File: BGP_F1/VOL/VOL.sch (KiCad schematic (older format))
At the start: 26 parts, among them P1 CONN_01X05, P2 CONN_01X05, P3 CONN_01X05, P4 CONN_01X03, P5 CONN_01X02, P6 CONN_02X02, P7 CONN_01X12, U1 MC33178, U2 MC33178

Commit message: F1 VOL Prot Diode
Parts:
- added D1: 1N4148, Diodes_SMD:D_SOD-123, symbol D_Small_ALT
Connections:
- net Earth: now also D1.2 (A)
- net V+: now also D1.1 (K)
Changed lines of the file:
@@
 LIBS:contrib
 LIBS:valves
-LIBS:vol-cache
+LIBS:VOL-cache
 EELAYER 25 0
 EELAYER END
@@
 Text Label 8400 3300 1    60   ~ 0
 V+
+$Comp
+L D_Small_ALT D1
+U 1 1 5A5F9F82
+P 8700 3400
+F 0 "D1" H 8650 3480 50  0000 L CNN
+F 1 "1N4148" H 8550 3320 50  0000 L CNN
+F 2 "Diodes_SMD:D_SOD-123" V 8700 3400 50  0001 C CNN
+F 3 "" V 8700 3400 50  0001 C CNN
+	1    8700 3400
+	0    1    1    0
+$EndComp
+Wire Wire Line
+	8400 3500 8700 3500
+Wire Wire Line
+	8400 3300 8700 3300
 $EndSCHEMATC

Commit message: F boards routed, various optimisations made
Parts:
- D1: footprint Diodes_SMD:D_SOD-123 -> Diodes_SMD:DO-214BA
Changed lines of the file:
@@
 F 0 "D1" H 8650 3480 50  0000 L CNN
 F 1 "1N4148" H 8550 3320 50  0000 L CNN
-F 2 "Diodes_SMD:D_SOD-123" V 8700 3400 50  0001 C CNN
+F 2 "Diodes_SMD:DO-214BA" V 8700 3400 50  0001 C CNN
 F 3 "" V 8700 3400 50  0001 C CNN
 	1    8700 3400

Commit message: F VOL
POT EARTH FIXUP
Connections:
- net Earth: now also P7.10 (P10)
- net Vref: no longer P7.10 (P10)
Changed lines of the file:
@@
 Text Label 9400 3350 2    60   ~ 0
 PV_3
-Text Label 9400 3150 2    60   ~ 0
-Vref
 Text Label 2650 4750 0    60   ~ 0
 V+
@@
 Wire Wire Line
 	8400 3300 8700 3300
+$Comp
+L Earth #PWR?
+U 1 1 5A606171
+P 9400 3150
+F 0 "#PWR?" H 9400 2900 50  0001 C CNN
+F 1 "Earth" H 9400 3000 50  0001 C CNN
+F 2 "" H 9400 3150 50  0000 C CNN
+F 3 "" H 9400 3150 50  0000 C CNN
+	1    9400 3150
+	0    1    1    0
+$EndComp
 $EndSCHEMATC

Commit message: Updated F_VOL
Using 10kB, 100kA pot with correct orientation, and pot correction for blend.
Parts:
- R3, R4: value 4.99k -> 11.1k
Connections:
- net PB1_1: now also P7.3 (P3); no longer P7.1 (P1)
- net PB1_2: no longer R3.1
- net PB2_2: no longer R4.1
- net Vref: now also P7.1 (P1), P7.6 (P6), R3.1, R4.1; no longer P7.3 (P3), P7.4 (P4)
- net PB2_3 renamed PB2_1
- net PB2_1: now also P7.4 (P4); no longer P7.6 (P6)
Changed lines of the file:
@@
 V+
 $Comp
-L Earth #PWR01
+L Earth #PWR5
 U 1 1 5A5EC7CD
 P 4150 3200
-F 0 "#PWR01" H 4150 2950 50  0001 C CNN
+F 0 "#PWR5" H 4150 2950 50  0001 C CNN
 F 1 "Earth" H 4150 3050 50  0001 C CNN
 F 2 "" H 4150 3200 50  0000 C CNN
@@
 Text Label 3650 3900 3    60   ~ 0
 Vref
-$Comp
-L R_Small R3
-U 1 1 5A5EC802
-P 4800 3500
-F 0 "R3" H 4830 3520 50  0000 L CNN
-F 1 "4.99k" H 4830 3460 50  0000 L CNN
-F 2 "Resistors_SMD:R_0603_HandSoldering" H 4800 3500 50  0001 C CNN
-F 3 "" H 4800 3500 50  0000 C CNN
-	1    4800 3500
-	0    1    1    0
-$EndComp
 Text Label 4700 3500 1    60   ~ 0
 PB1_1
-Text Label 5050 3500 1    60   ~ 0
+Text Label 4900 3500 1    60   ~ 0
 PB1_2
 Text Label 3650 3600 2    60   ~ 0
@@
 V+
 $Comp
-L Earth #PWR02
+L Earth #PWR6
 U 1 1 5A5EC9DD
 P 4150 4200
-F 0 "#PWR02" H 4150 3950 50  0001 C CNN
+F 0 "#PWR6" H 4150 3950 50  0001 C CNN
 F 1 "Earth" H 4150 4050 50  0001 C CNN
 F 2 "" H 4150 4200 50  0000 C CNN
@@
 Text Label 3650 4900 3    60   ~ 0
 Vref
-$Comp
-L R_Small R4
-U 1 1 5A5EC9E9
-P 4800 4500
-F 0 "R4" H 4830 4520 50  0000 L CNN
-F 1 "4.99k" H 4830 4460 50  0000 L CNN
-F 2 "Resistors_SMD:R_0603_HandSoldering" H 4800 4500 50  0001 C CNN
-F 3 "" H 4800 4500 50  0000 C CNN
-	1    4800 4500
-	0    1    1    0
-$EndComp
-Text Label 5050 4500 1    60   ~ 0
+Text Label 4900 4500 1    60   ~ 0
 PB2_2
 Text Label 3650 4600 2    60   ~ 0
@@
 V+
 $Comp
-L Earth #PWR03
+L Earth #PWR7
 U 1 1 5A5ECE8B
 P 5850 2750
-F 0 "#PWR03" H 5850 2500 50  0001 C CNN
+F 0 "#PWR7" H 5850 2500 50  0001 C CNN
 F 1 "Earth" H 5850 2600 50  0001 C CNN
 F 2 "" H 5850 2750 50  0000 C CNN
@@
 $EndComp
 $Comp
-L Earth #PWR04
+L Earth #PWR8
 U 1 1 5A5ED3C7
 P 6800 3600
-F 0 "#PWR04" H 6800 3350 50  0001 C CNN
+F 0 "#PWR8" H 6800 3350 50  0001 C CNN
 F 1 "Earth" H 6800 3450 50  0001 C CNN
 F 2 "" H 6800 3600 50  0000 C CNN
@@
 V+
 $Comp
-L Earth #PWR05
+L Earth #PWR10
 U 1 1 5A5EDC55
 P 7950 2650
-F 0 "#PWR05" H 7950 2400 50  0001 C CNN
+F 0 "#PWR10" H 7950 2400 50  0001 C CNN
 F 1 "Earth" H 7950 2500 50  0001 C CNN
 F 2 "" H 7950 2650 50  0000 C CNN
@@
 Connection ~ 7450 3050
 $Comp
-L Earth #PWR06
+L Earth #PWR9
 U 1 1 5A5EE012
 P 7450 3550
-F 0 "#PWR06" H 7450 3300 50  0001 C CNN
+F 0 "#PWR9" H 7450 3300 50  0001 C CNN
 F 1 "Earth" H 7450 3400 50  0001 C CNN
 F 2 "" H 7450 3550 50  0000 C CNN
@@
 OUT_N
 $Comp
-L Earth #PWR07
+L Earth #PWR1
 U 1 1 5A5EEAF2
 P 2650 2550
-F 0 "#PWR07" H 2650 2300 50  0001 C CNN
+F 0 "#PWR1" H 2650 2300 50  0001 C CNN
 F 1 "Earth" H 2650 2400 50  0001 C CNN
 F 2 "" H 2650 2550 50  0000 C CNN
@@
 $EndComp
 $Comp
-L Earth #PWR08
+L Earth #PWR2
 U 1 1 5A5EEB70
 P 2650 3150
-F 0 "#PWR08" H 2650 2900 50  0001 C CNN
+F 0 "#PWR2" H 2650 2900 50  0001 C CNN
 F 1 "Earth" H 2650 3000 50  0001 C CNN
 F 2 "" H 2650 3150 50  0000 C CNN
@@
 $EndComp
 $Comp
-L Earth #PWR09
+L Earth #PWR3
 U 1 1 5A5EEBC0
 P 2650 3750
-F 0 "#PWR09" H 2650 3500 50  0001 C CNN
+F 0 "#PWR3" H 2650 3500 50  0001 C CNN
 F 1 "Earth" H 2650 3600 50  0001 C CNN
 F 2 "" H 2650 3750 50  0000 C CNN
@@
 OUT
 $Comp
-L Earth #PWR010
+L Earth #PWR4
 U 1 1 5A5EF35E
 P 2650 4050
-F 0 "#PWR010" H 2650 3800 50  0001 C CNN
+F 0 "#PWR4" H 2650 3800 50  0001 C CNN
 F 1 "Earth" H 2650 3900 50  0001 C CNN
 F 2 "" H 2650 4050 50  0000 C CNN
@@
 	1    0    0    -1
 $EndComp
-Text Label 9400 2250 2    60   ~ 0
+Text Label 9400 2450 2    60   ~ 0
 PB1_1
 Text Label 9400 2350 2    60   ~ 0
@@
 Text Label 9400 2650 2    60   ~ 0
 PB2_2
-Text Label 9400 2750 2    60   ~ 0
-PB2_3
+Text Label 9400 2550 2    60   ~ 0
+PB2_1
 Text Label 9400 3250 2    60   ~ 0
 PV_2
@@
 BUF_N
 Text Label 4700 4500 1    60   ~ 0
-PB2_3
-Text Label 9400 2450 2    60   ~ 0
-Vref
-Text Label 9400 2550 2    60   ~ 0
+PB2_1
+Text Label 9400 2250 2    60   ~ 0
+Vref
+Text Label 9400 2750 2    60   ~ 0
 Vref
 Text Label 9400 3350 2    60   ~ 0
@@
 $EndComp
 $Comp
-L Earth #PWR011
+L Earth #PWR11
 U 1 1 5A5F15E8
 P 8400 3500
-F 0 "#PWR011" H 8400 3250 50  0001 C CNN
+F 0 "#PWR11" H 8400 3250 50  0001 C CNN
 F 1 "Earth" H 8400 3350 50  0001 C CNN
 F 2 "" H 8400 3500 50  0000 C CNN
@@
 	8400 3300 8700 3300
 $Comp
-L Earth #PWR?
+L Earth #PWR12
 U 1 1 5A606171
 P 9400 3150
-F 0 "#PWR?" H 9400 2900 50  0001 C CNN
+F 0 "#PWR12" H 9400 2900 50  0001 C CNN
 F 1 "Earth" H 9400 3000 50  0001 C CNN
 F 2 "" H 9400 3150 50  0000 C CNN
@@
 	0    1    1    0
 $EndComp
+$Comp
+L R_Small R3
+U 1 1 5A6282A9
+P 4700 3650
+F 0 "R3" H 4730 3670 50  0000 L CNN
+F 1 "11.1k" H 4730 3610 50  0000 L CNN
+F 2 "Resistors_SMD:R_0603_HandSoldering" H 4700 3650 50  0001 C CNN
+F 3 "" H 4700 3650 50  0000 C CNN
+	1    4700 3650
+	-1   0    0    1
+$EndComp
+$Comp
+L R_Small R4
+U 1 1 5A628323
+P 4700 4650
+F 0 "R4" H 4730 4670 50  0000 L CNN
+F 1 "11.1k" H 4730 4610 50  0000 L CNN
+F 2 "Resistors_SMD:R_0603_HandSoldering" H 4700 4650 50  0001 C CNN
+F 3 "" H 4700 4650 50  0000 C CNN
+	1    4700 4650
+	-1   0    0    1
+$EndComp
+Text Label 4700 4800 3    60   ~ 0
+Vref
+Wire Wire Line
+	4700 4800 4700 4750
+Wire Wire Line
+	4700 4500 4700 4550
+Wire Wire Line
+	4700 3500 4700 3550
+Wire Wire Line
+	4700 3800 4700 3750
+Text Label 4700 3800 3    60   ~ 0
+Vref
 $EndSCHEMATC

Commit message: New F0 Version
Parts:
- P1, P2, P3: footprint Connectors_Molex:Molex_MicroLatch-53253-0570_05x2.00mm_Straight -> Connectors_JST:JST_PH_B5B-PH-K_05x2.00mm_Straight
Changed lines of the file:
@@
 V+
 $Comp
-L Earth #PWR5
+L Earth #PWR01
 U 1 1 5A5EC7CD
 P 4150 3200
-F 0 "#PWR5" H 4150 2950 50  0001 C CNN
+F 0 "#PWR01" H 4150 2950 50  0001 C CNN
 F 1 "Earth" H 4150 3050 50  0001 C CNN
 F 2 "" H 4150 3200 50  0000 C CNN
@@
 V+
 $Comp
-L Earth #PWR6
+L Earth #PWR02
 U 1 1 5A5EC9DD
 P 4150 4200
-F 0 "#PWR6" H 4150 3950 50  0001 C CNN
+F 0 "#PWR02" H 4150 3950 50  0001 C CNN
 F 1 "Earth" H 4150 4050 50  0001 C CNN
 F 2 "" H 4150 4200 50  0000 C CNN
@@
 V+
 $Comp
-L Earth #PWR7
+L Earth #PWR03
 U 1 1 5A5ECE8B
 P 5850 2750
-F 0 "#PWR7" H 5850 2500 50  0001 C CNN
+F 0 "#PWR03" H 5850 2500 50  0001 C CNN
 F 1 "Earth" H 5850 2600 50  0001 C CNN
 F 2 "" H 5850 2750 50  0000 C CNN
@@
 $EndComp
 $Comp
-L Earth #PWR8
+L Earth #PWR04
 U 1 1 5A5ED3C7
 P 6800 3600
-F 0 "#PWR8" H 6800 3350 50  0001 C CNN
+F 0 "#PWR04" H 6800 3350 50  0001 C CNN
 F 1 "Earth" H 6800 3450 50  0001 C CNN
 F 2 "" H 6800 3600 50  0000 C CNN
@@
 V+
 $Comp
-L Earth #PWR10
+L Earth #PWR05
 U 1 1 5A5EDC55
 P 7950 2650
-F 0 "#PWR10" H 7950 2400 50  0001 C CNN
+F 0 "#PWR05" H 7950 2400 50  0001 C CNN
 F 1 "Earth" H 7950 2500 50  0001 C CNN
 F 2 "" H 7950 2650 50  0000 C CNN
@@
 Connection ~ 7450 3050
 $Comp
-L Earth #PWR9
+L Earth #PWR06
 U 1 1 5A5EE012
 P 7450 3550
-F 0 "#PWR9" H 7450 3300 50  0001 C CNN
+F 0 "#PWR06" H 7450 3300 50  0001 C CNN
 F 1 "Earth" H 7450 3400 50  0001 C CNN
 F 2 "" H 7450 3550 50  0000 C CNN
@@
 F 0 "P1" H 2450 2650 50  0000 C CNN
 F 1 "CONN_01X05" V 2550 2350 50  0000 C CNN
-F 2 "Connectors_Molex:Molex_MicroLatch-53253-0570_05x2.00mm_Straight" H 2450 2350 50  0001 C CNN
+F 2 "Connectors_JST:JST_PH_B5B-PH-K_05x2.00mm_Straight" H 2450 2350 50  0001 C CNN
 F 3 "" H 2450 2350 50  0000 C CNN
 	1    2450 2350
@@
 F 0 "P2" H 2450 3250 50  0000 C CNN
 F 1 "CONN_01X05" V 2550 2950 50  0000 C CNN
-F 2 "Connectors_Molex:Molex_MicroLatch-53253-0570_05x2.00mm_Straight" H 2450 2950 50  0001 C CNN
+F 2 "Connectors_JST:JST_PH_B5B-PH-K_05x2.00mm_Straight" H 2450 2950 50  0001 C CNN
 F 3 "" H 2450 2950 50  0000 C CNN
 	1    2450 2950
@@
 F 0 "P3" H 2450 3850 50  0000 C CNN
 F 1 "CONN_01X05" V 2550 3550 50  0000 C CNN
-F 2 "Connectors_Molex:Molex_MicroLatch-53253-0570_05x2.00mm_Straight" H 2450 3550 50  0001 C CNN
+F 2 "Connectors_JST:JST_PH_B5B-PH-K_05x2.00mm_Straight" H 2450 3550 50  0001 C CNN
 F 3 "" H 2450 3550 50  0000 C CNN
 	1    2450 3550
@@
 OUT_N
 $Comp
-L Earth #PWR1
+L Earth #PWR07
 U 1 1 5A5EEAF2
 P 2650 2550
-F 0 "#PWR1" H 2650 2300 50  0001 C CNN
+F 0 "#PWR07" H 2650 2300 50  0001 C CNN
 F 1 "Earth" H 2650 2400 50  0001 C CNN
 F 2 "" H 2650 2550 50  0000 C CNN
@@
 $EndComp
 $Comp
-L Earth #PWR2
+L Earth #PWR08
 U 1 1 5A5EEB70
 P 2650 3150
-F 0 "#PWR2" H 2650 2900 50  0001 C CNN
+F 0 "#PWR08" H 2650 2900 50  0001 C CNN
 F 1 "Earth" H 2650 3000 50  0001 C CNN
 F 2 "" H 2650 3150 50  0000 C CNN
@@
 $EndComp
 $Comp
-L Earth #PWR3
+L Earth #PWR09
 U 1 1 5A5EEBC0
 P 2650 3750
-F 0 "#PWR3" H 2650 3500 50  0001 C CNN
+F 0 "#PWR09" H 2650 3500 50  0001 C CNN
 F 1 "Earth" H 2650 3600 50  0001 C CNN
 F 2 "" H 2650 3750 50  0000 C CNN
@@
 OUT
 $Comp
-L Earth #PWR4
+L Earth #PWR010
 U 1 1 5A5EF35E
 P 2650 4050
-F 0 "#PWR4" H 2650 3800 50  0001 C CNN
+F 0 "#PWR010" H 2650 3800 50  0001 C CNN
 F 1 "Earth" H 2650 3900 50  0001 C CNN
 F 2 "" H 2650 4050 50  0000 C CNN
@@
 $EndComp
 $Comp
-L Earth #PWR11
+L Earth #PWR011
 U 1 1 5A5F15E8
 P 8400 3500
-F 0 "#PWR11" H 8400 3250 50  0001 C CNN
+F 0 "#PWR011" H 8400 3250 50  0001 C CNN
 F 1 "Earth" H 8400 3350 50  0001 C CNN
 F 2 "" H 8400 3500 50  0000 C CNN
@@
 	8400 3300 8700 3300
 $Comp
-L Earth #PWR12
+L Earth #PWR012
 U 1 1 5A606171
 P 9400 3150
-F 0 "#PWR12" H 9400 2900 50  0001 C CNN
+F 0 "#PWR012" H 9400 2900 50  0001 C CNN
 F 1 "Earth" H 9400 3000 50  0001 C CNN
 F 2 "" H 9400 3150 50  0000 C CNN

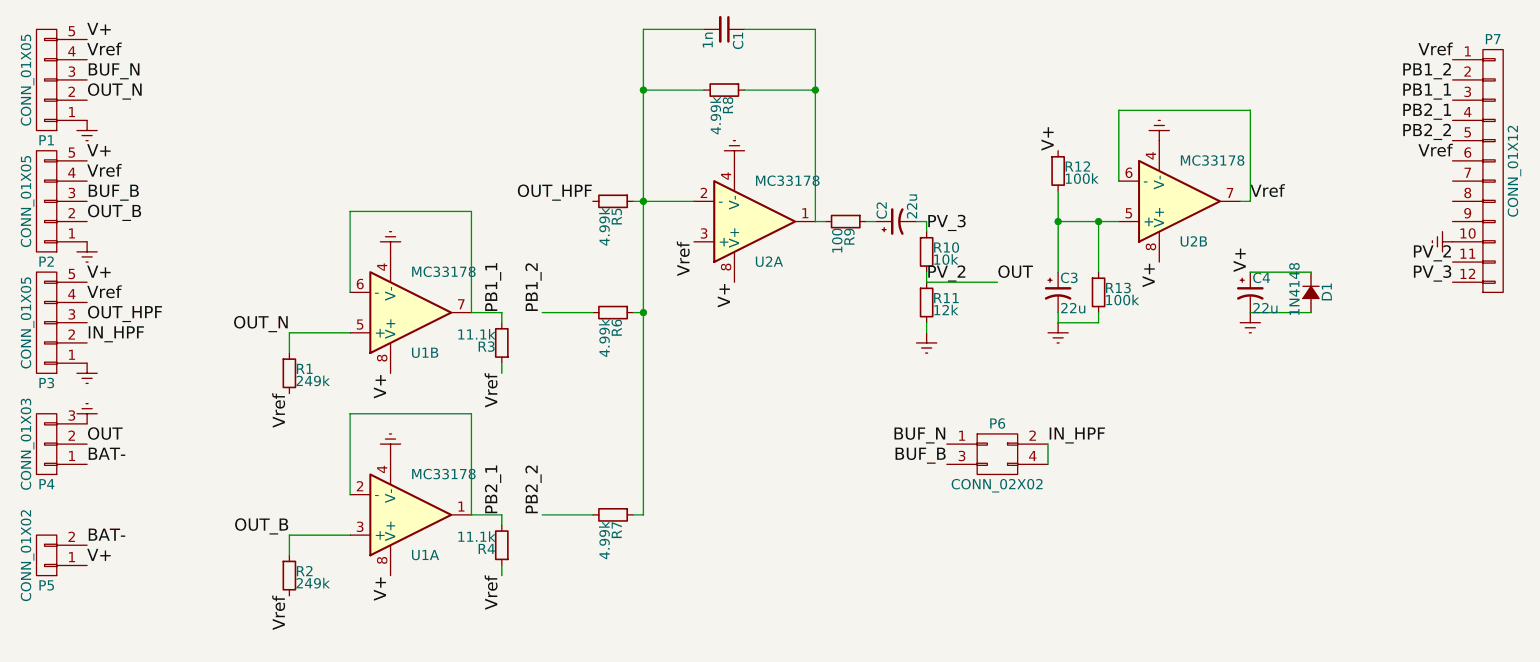
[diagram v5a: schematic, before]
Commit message: F1 updates to reverse pots
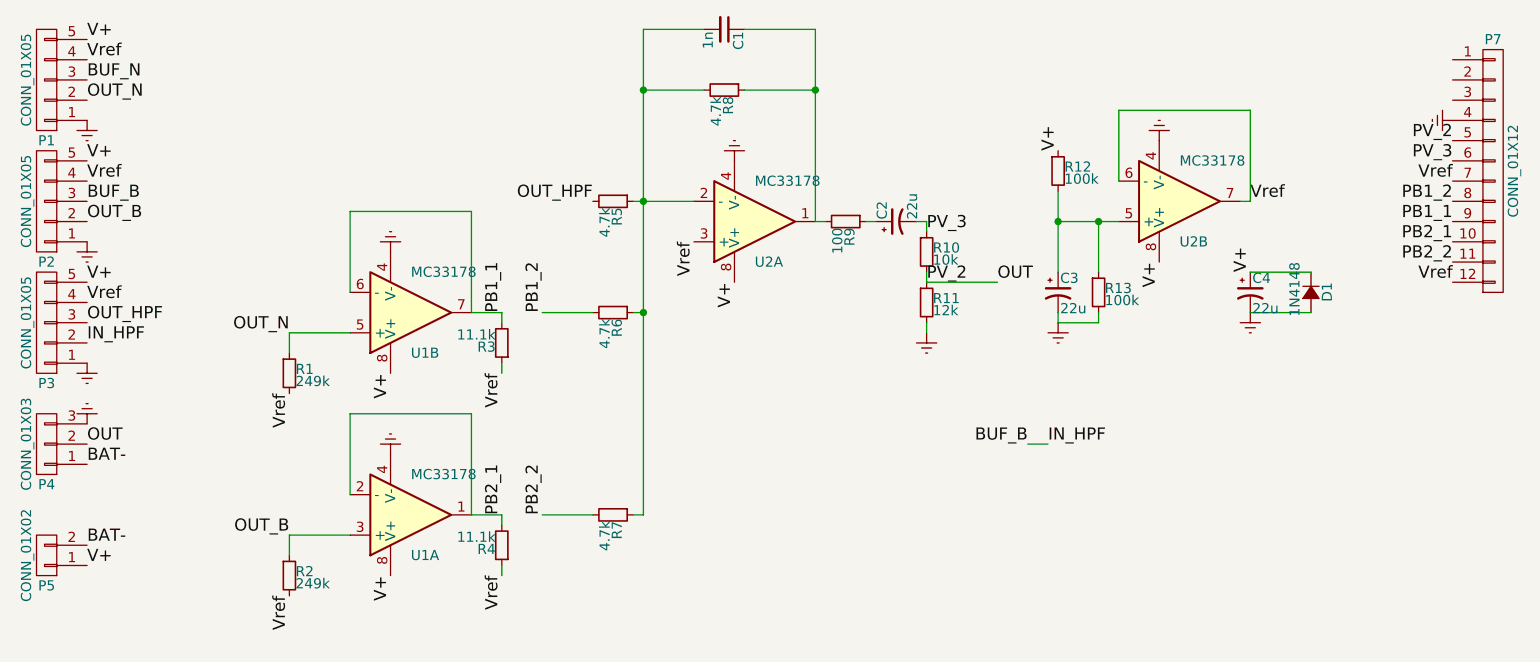
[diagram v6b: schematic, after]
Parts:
- removed P6: CONN_02X02, Pin_Headers:Pin_Header_Straight_2x02, symbol CONN_02X02
- R5, R6, R7, R8: value 4.99k -> 4.7k
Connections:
- net IN_HPF is gone; now on net BUF_B: P3.2 (P2)
- net Earth: now also P7.4 (P4); no longer P7.10 (P10)
- net OUT: now also P7.5 (P5); no longer P7.11 (P11)
- net PB1_1: now also P7.9 (P9); no longer P7.3 (P3)
- net PB1_2: now also P7.8 (P8); no longer P7.2 (P2)
- net PB2_1: now also P7.10 (P10); no longer P7.4 (P4)
- net PB2_2: now also P7.11 (P11); no longer P7.5 (P5)
- net PV_3: now also P7.6 (P6); no longer P7.12 (P12)
- net Vref: now also P7.12 (P12), P7.7 (P7); no longer P7.1 (P1), P7.6 (P6)
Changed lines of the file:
@@
 P 5250 3500
 F 0 "R6" H 5280 3520 50  0000 L CNN
-F 1 "4.99k" H 5280 3460 50  0000 L CNN
+F 1 "4.7k" H 5280 3460 50  0000 L CNN
 F 2 "Resistors_SMD:R_0603_HandSoldering" H 5250 3500 50  0001 C CNN
 F 3 "" H 5250 3500 50  0000 C CNN
@@
 P 5250 4500
 F 0 "R7" H 5280 4520 50  0000 L CNN
-F 1 "4.99k" H 5280 4460 50  0000 L CNN
+F 1 "4.7k" H 5280 4460 50  0000 L CNN
 F 2 "Resistors_SMD:R_0603_HandSoldering" H 5250 4500 50  0001 C CNN
 F 3 "" H 5250 4500 50  0000 C CNN
@@
 P 5250 2950
 F 0 "R5" H 5280 2970 50  0000 L CNN
-F 1 "4.99k" H 5280 2910 50  0000 L CNN
+F 1 "4.7k" H 5280 2910 50  0000 L CNN
 F 2 "Resistors_SMD:R_0603_HandSoldering" H 5250 2950 50  0001 C CNN
 F 3 "" H 5250 2950 50  0000 C CNN
@@
 P 5800 2400
 F 0 "R8" H 5830 2420 50  0000 L CNN
-F 1 "4.99k" H 5830 2360 50  0000 L CNN
+F 1 "4.7k" H 5830 2360 50  0000 L CNN
 F 2 "Resistors_SMD:R_0603_HandSoldering" H 5800 2400 50  0001 C CNN
 F 3 "" H 5800 2400 50  0000 C CNN
@@
 	1    0    0    -1
 $EndComp
-Text Label 9400 2450 2    60   ~ 0
+Text Label 9400 3050 2    60   ~ 0
 PB1_1
-Text Label 9400 2350 2    60   ~ 0
+Text Label 9400 2950 2    60   ~ 0
 PB1_2
+Text Label 9400 3250 2    60   ~ 0
+PB2_2
+Text Label 9400 3150 2    60   ~ 0
+PB2_1
 Text Label 9400 2650 2    60   ~ 0
-PB2_2
-Text Label 9400 2550 2    60   ~ 0
-PB2_1
-Text Label 9400 3250 2    60   ~ 0
 PV_2
-$Comp
-L CONN_02X02 P6
-U 1 1 5A5EF9B3
-P 7150 4200
-F 0 "P6" H 7150 4350 50  0000 C CNN
-F 1 "CONN_02X02" H 7150 4050 50  0000 C CNN
-F 2 "Pin_Headers:Pin_Header_Straight_2x02" H 7150 3000 50  0001 C CNN
-F 3 "" H 7150 3000 50  0000 C CNN
-	1    7150 4200
-	1    0    0    -1
-$EndComp
 Text Label 7400 4150 0    60   ~ 0
 IN_HPF
-Wire Wire Line
-	7400 4250 7400 4150
-Text Label 6900 4250 2    60   ~ 0
-BUF_B
-Text Label 6900 4150 2    60   ~ 0
-BUF_N
 Text Label 4700 4500 1    60   ~ 0
 PB2_1
-Text Label 9400 2250 2    60   ~ 0
+Text Label 9400 2850 2    60   ~ 0
+Vref
+Text Label 9400 3350 2    60   ~ 0
 Vref
 Text Label 9400 2750 2    60   ~ 0
-Vref
-Text Label 9400 3350 2    60   ~ 0
 PV_3
 Text Label 2650 4750 0    60   ~ 0
@@
 L Earth #PWR012
 U 1 1 5A606171
-P 9400 3150
-F 0 "#PWR012" H 9400 2900 50  0001 C CNN
-F 1 "Earth" H 9400 3000 50  0001 C CNN
-F 2 "" H 9400 3150 50  0000 C CNN
-F 3 "" H 9400 3150 50  0000 C CNN
-	1    9400 3150
+P 9400 2550
+F 0 "#PWR012" H 9400 2300 50  0001 C CNN
+F 1 "Earth" H 9400 2400 50  0001 C CNN
+F 2 "" H 9400 2550 50  0000 C CNN
+F 3 "" H 9400 2550 50  0000 C CNN
+	1    9400 2550
 	0    1    1    0
 $EndComp
@@
 Text Label 4700 3800 3    60   ~ 0
 Vref
+Text Label 7300 4150 2    60   ~ 0
+BUF_B
+Wire Wire Line
+	7300 4150 7400 4150
 $EndSCHEMATC

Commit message: HPF Done
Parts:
- removed R3, R4: 11.1k, Resistors_SMD:R_0603_HandSoldering, symbol R_Small
- C1: value 1n -> 100p; footprint Capacitors_SMD:C_0805_HandSoldering -> Capacitors_SMD:C_0805
- D1: footprint Diodes_SMD:DO-214BA -> Diodes_SMD:SOD-123
- P1: footprint Connectors_JST:JST_PH_B5B-PH-K_05x2.00mm_Straight -> Diodes_SMD:SMA_Standard
- R1, R2: value 249k -> 100; footprint Resistors_SMD:R_0603_HandSoldering -> Resistors_SMD:R_0603
- R10: renamed from R12; footprint Resistors_SMD:R_0603_HandSoldering -> Resistors_SMD:R_0603
- R11: renamed from R13; footprint Resistors_SMD:R_0603_HandSoldering -> Resistors_SMD:R_0603
- R3: renamed from R5; value 4.7k -> 47k; footprint Resistors_SMD:R_0603_HandSoldering -> Resistors_SMD:R_0603
- R4: renamed from R6; value 4.7k -> 47k; footprint Resistors_SMD:R_0603_HandSoldering -> Resistors_SMD:R_0603
- R5: renamed from R7; value 4.7k -> 47k; footprint Resistors_SMD:R_0603_HandSoldering -> Resistors_SMD:R_0603
- R6: renamed from R8; value 4.7k -> 47k; footprint Resistors_SMD:R_0603_HandSoldering -> Resistors_SMD:R_0603
- R7: renamed from R9; footprint Resistors_SMD:R_0603_HandSoldering -> Resistors_SMD:R_0603
- R8: renamed from R10; footprint Resistors_SMD:R_0603_HandSoldering -> Resistors_SMD:R_0603
- R9: renamed from R11; footprint Resistors_SMD:R_0603_HandSoldering -> Resistors_SMD:R_0603
- renumbered P7 to P6
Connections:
- net BUF_B: no longer P3.2 (P2)
- net BUF_N: now also P3.2 (P2)
- net OUT_B: now also R2.2; no longer R2.1, U1.3 (+)
- net OUT_N: now also R1.2; no longer R1.1, U1.5 (+)
- net PB1_1: now also U1.1, U1.2 (-); no longer U1.6 (-), U1.7
- net PB2_1: now also U1.6 (-), U1.7; no longer U1.1, U1.2 (-)
- net Vref: now also U2.1, U2.2 (-), U2.5 (+); no longer R1.2, R2.2, U2.3 (+), U2.6 (-), U2.7
- net at C1.2, R3.1, R4.1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: now also U2.6 (-); no longer U2.2 (-)
- net at C1.1, R6.1, R7.2: now also U2.7; no longer U2.1
- net at C3.1, R10.2, R11.1: now also U2.3 (+); no longer U2.5 (+)
- new net: R2.1, U1.5 (+)
- new net: R1.1, U1.3 (+)
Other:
- moved on the sheet: U2A, U2B
